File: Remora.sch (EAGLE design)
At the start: 81 parts, among them IC1 MCP23017, J2 GROVE-I2C, P1 PADSMALL, T1 2N3904, T2 BSS138

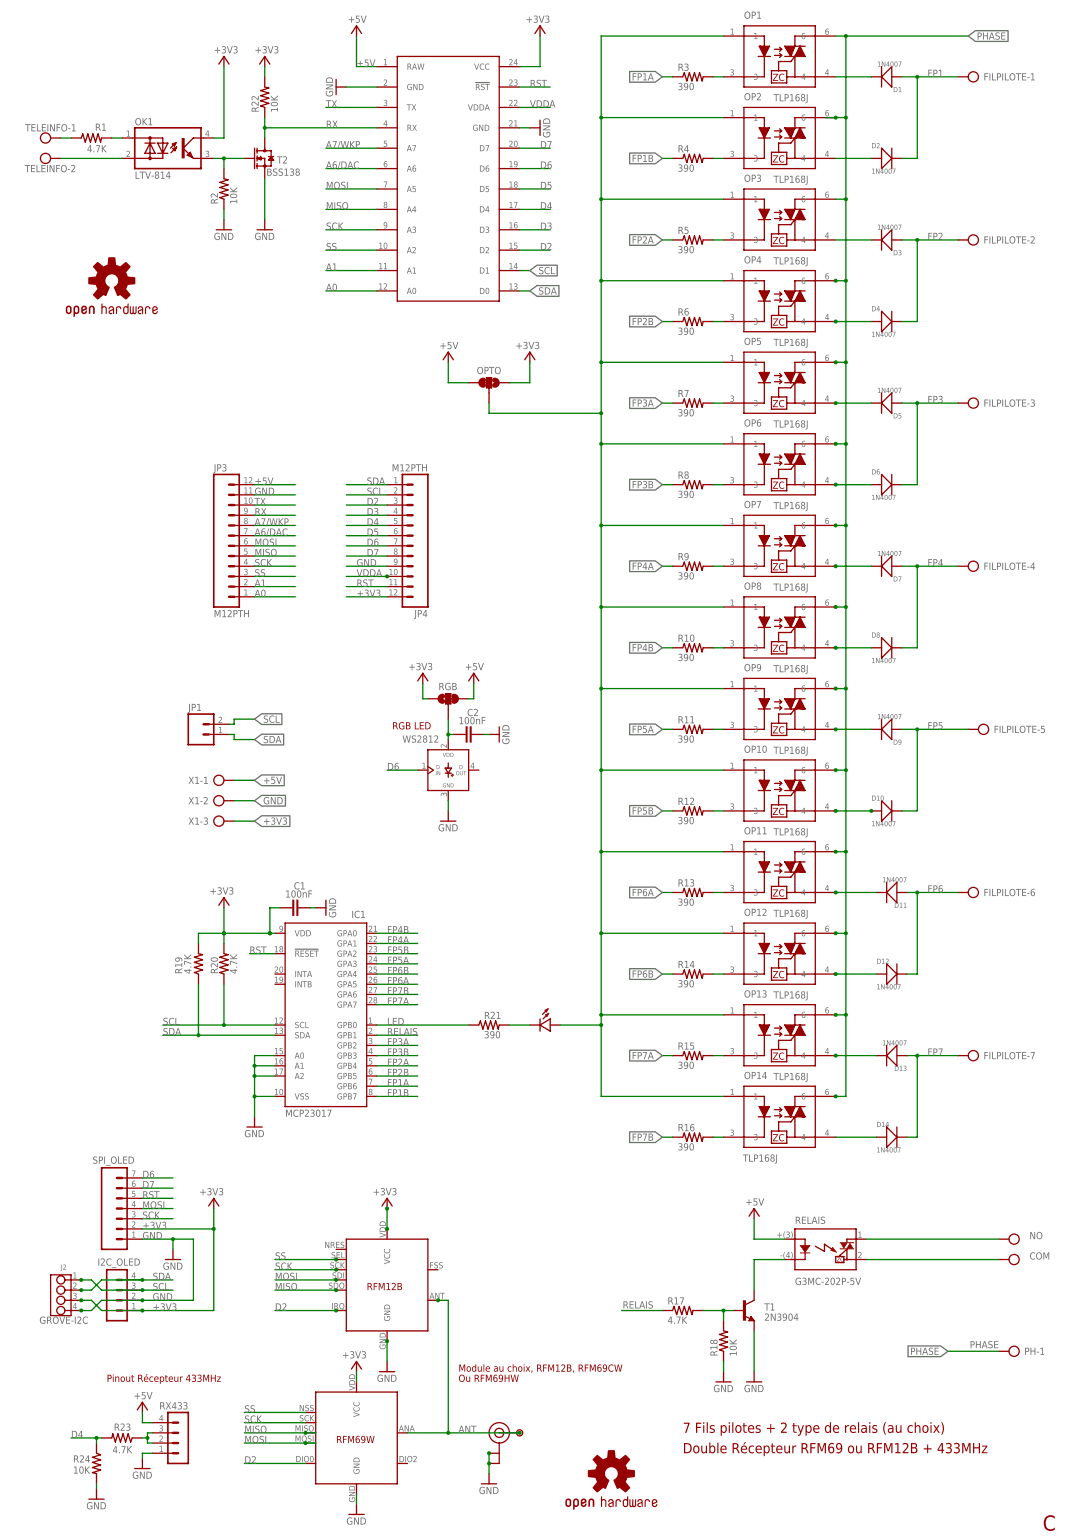
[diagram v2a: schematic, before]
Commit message: Modification de la Remora pour accepter directement un Wemos D1 mini sur headers
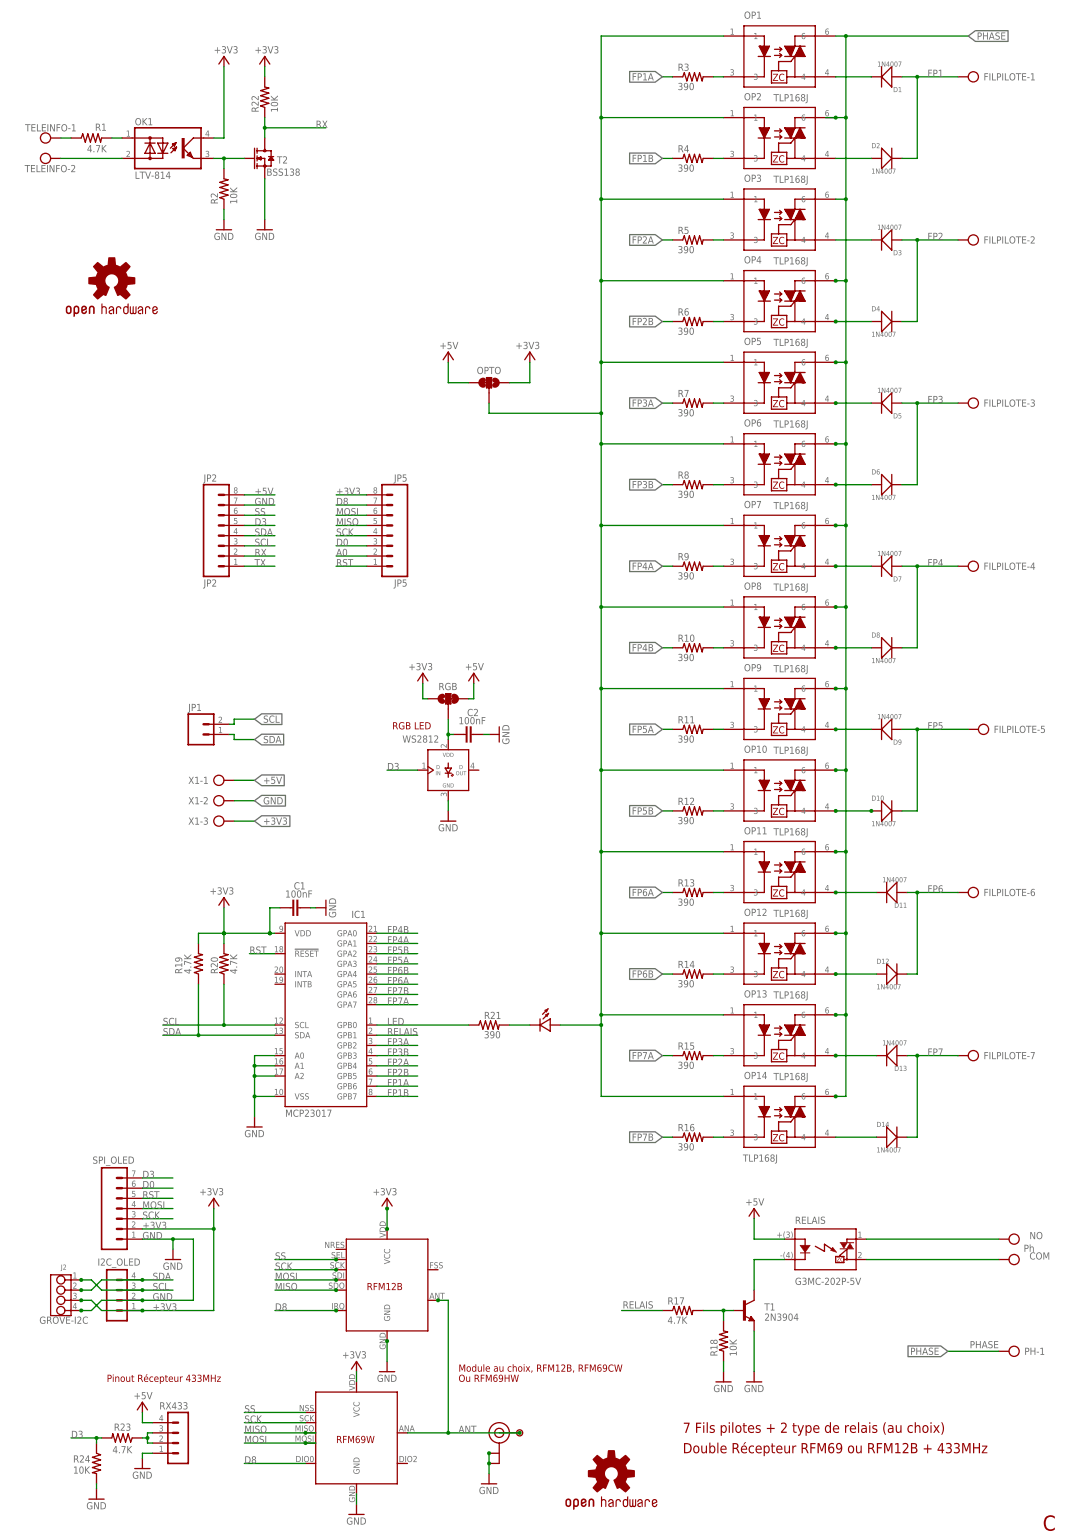
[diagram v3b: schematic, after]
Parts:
- removed JP3, JP4: M12PTH, Spark:M12PTH
- removed PARTICLE: Spark/Photon, Spark:SPARK_CORECORE
- added JP2: JP2, SparkFun:M081X08
- added JP5: JP5, SparkFun:M081X08
- PH: value (none) -> Ph
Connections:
- removed net A1: JP3.2, PARTICLE.A1
- removed net A6/DAC: JP3.7, PARTICLE.A6
- removed net A7/WKP: JP3.8, PARTICLE.A7
- removed net D2: JP4.3, PARTICLE.D2, U$2.IRQ, U$3.DIO0
- removed net D4: JP4.5, PARTICLE.D4, R23.2, R24.1
- removed net D5: JP4.6, PARTICLE.D5
- removed net D6: JP4.7, PARTICLE.D6, SPI_OLED.7, WS2812.DIN
- removed net D7: JP4.8, PARTICLE.D7, SPI_OLED.6
- removed net VDDA: JP4.10, PARTICLE.VDDA
- new net D0: JP5.3, SPI_OLED.6
- new net D8: JP5.7, U$2.IRQ, U$3.DIO0
- net +3V3: now also JP5.8; no longer JP4.12, PARTICLE.VCC
- net +5V: now also JP2.8; no longer JP3.12, PARTICLE.RAW
- net A0: now also JP5.2; no longer JP3.1, PARTICLE.A0
- net D3: now also JP2.5, R23.2, R24.1, SPI_OLED.7, WS2812.DIN; no longer JP4.4, PARTICLE.D3
- net GND: now also JP2.7; no longer JP3.11, JP4.9, PARTICLE.GND@2, PARTICLE.GND@21
- net MISO: now also JP5.5; no longer JP3.5, PARTICLE.A4
- net MOSI: now also JP5.6; no longer JP3.6, PARTICLE.A5
- net RST: now also JP5.1; no longer JP4.11, PARTICLE.!RST
- net RX: now also JP2.2; no longer JP3.9, PARTICLE.RX
- net SCK: now also JP5.4; no longer JP3.4, PARTICLE.A3
- net SCL: now also JP2.3; no longer JP4.2, PARTICLE.D1
- net SDA: now also JP2.4; no longer JP4.1, PARTICLE.D0
- net SS: now also JP2.6; no longer JP3.3, PARTICLE.A2
- net TX: now also JP2.1; no longer JP3.10, PARTICLE.TX

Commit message: Mise à jour du numéro de version du PCB
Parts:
- PH: value Ph -> (none)
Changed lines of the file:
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@@
 <part name="X1" library="con-ptr500" deviceset="AK500/3" device=""/>
 <part name="JP1" library="SparkFun-Connectors" deviceset="M02" device="PTH"/>
-<part name="PH" library="con-ptr500" deviceset="AK500/3" device="" value="Ph"/>
+<part name="PH" library="con-ptr500" deviceset="AK500/3" device=""/>
 <part name="RELAIS" library="sip-4" deviceset="G3MC-202P" device="" value="G3MC-202P-5V"/>
 <part name="JP2" library="SparkFun" deviceset="M08" device="1X08" value="JP2"/>
